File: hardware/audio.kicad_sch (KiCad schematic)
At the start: 5 parts, among them J10 AudioJack_PJ-342

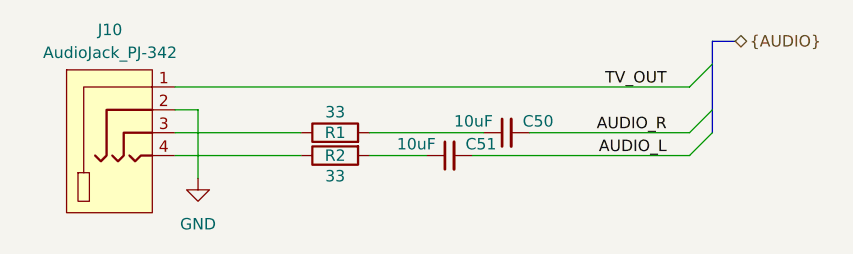
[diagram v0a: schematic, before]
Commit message: Finished DC DC converters and started decoupling the CPU
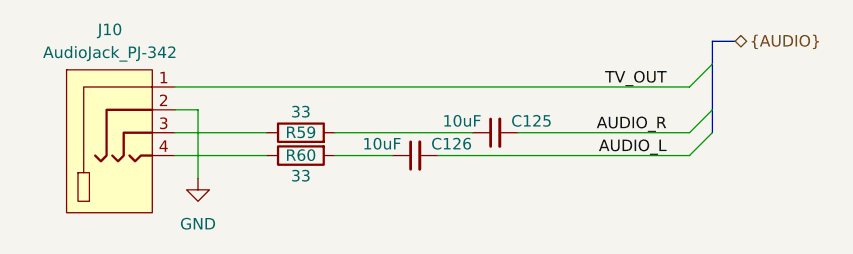
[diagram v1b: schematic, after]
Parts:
- renumbered C50 to C125, C51 to C126, R1 to R59, R2 to R60
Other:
- moved on the sheet: C125, C126, R59, R60
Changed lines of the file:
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@@
 	(wire
 		(pts
-			(xy 132.08 95.25) (xy 146.05 95.25)
-		)
-		(stroke
-			(width 0)
-			(type default)
-		)
-	)
-	(wire
-		(pts
-			(xy 165.1 95.25) (xy 189.23 95.25)
+			(xy 132.08 95.25) (xy 142.24 95.25)
+		)
+		(stroke
+			(width 0)
+			(type default)
+		)
+	)
+	(wire
+		(pts
+			(xy 161.29 95.25) (xy 189.23 95.25)
 		)
 		(stroke
@@
 	(wire
 		(pts
-			(xy 153.67 92.71) (xy 166.37 92.71)
+			(xy 149.86 92.71) (xy 165.1 92.71)
 		)
 		(stroke
@@
 	(wire
 		(pts
-			(xy 153.67 95.25) (xy 160.02 95.25)
+			(xy 149.86 95.25) (xy 156.21 95.25)
 		)
 		(stroke
@@
 	(wire
 		(pts
-			(xy 171.45 92.71) (xy 189.23 92.71)
+			(xy 170.18 92.71) (xy 189.23 92.71)
 		)
 		(stroke
@@
 	(wire
 		(pts
-			(xy 132.08 92.71) (xy 146.05 92.71)
+			(xy 132.08 92.71) (xy 142.24 92.71)
 		)
 		(stroke
@@
 	(symbol
 		(lib_id "Device:R")
-		(at 149.86 95.25 90)
+		(at 146.05 95.25 90)
 		(mirror x)
 		(unit 1)
@@
 		(on_board yes)
 		(dnp no)
-		(property "Reference" "R2"
-			(at 149.86 95.25 90)
+		(property "Reference" "R60"
+			(at 146.05 95.25 90)
 			(effects
 				(font
@@
 		)
 		(property "Value" "33"
-			(at 149.86 97.536 90)
+			(at 146.05 97.536 90)
 			(effects
 				(font
@@
 		)
 		(property "Footprint" "Resistor_SMD:R_0402_1005Metric"
-			(at 149.86 93.472 90)
+			(at 146.05 93.472 90)
 			(effects
 				(font
@@
 		)
 		(property "Datasheet" "~"
-			(at 149.86 95.25 0)
+			(at 146.05 95.25 0)
 			(effects
 				(font
@@
 		)
 		(property "Description" "Resistor"
-			(at 149.86 95.25 0)
+			(at 146.05 95.25 0)
 			(effects
 				(font
@@
 		)
 		(property "LCSC Part #" ""
-			(at 149.86 95.25 90)
+			(at 146.05 95.25 90)
 			(effects
 				(font
@@
 			(project "cm0"
 				(path "/b53f5dbb-8078-4818-9e8f-fdf90ba6d854/5ae223d4-d68f-4671-997c-b9179dc72885"
-					(reference "R2")
+					(reference "R60")
 					(unit 1)
 				)
@@
 	(symbol
 		(lib_id "Device:C_Small")
-		(at 168.91 92.71 90)
+		(at 167.64 92.71 90)
 		(unit 1)
 		(exclude_from_sim no)
@@
 		(on_board yes)
 		(dnp no)
-		(property "Reference" "C50"
-			(at 170.688 91.44 90)
+		(property "Reference" "C125"
+			(at 169.418 91.44 90)
 			(effects
 				(font
@@
 		)
 		(property "Value" "10uF"
-			(at 167.386 91.44 90)
+			(at 166.116 91.44 90)
 			(effects
 				(font
@@
 		)
 		(property "Footprint" "Capacitor_SMD:C_0603_1608Metric"
-			(at 168.91 92.71 0)
+			(at 167.64 92.71 0)
 			(effects
 				(font
@@
 		)
 		(property "Datasheet" "~"
-			(at 168.91 92.71 0)
+			(at 167.64 92.71 0)
 			(effects
 				(font
@@
 		)
 		(property "Description" "Unpolarized capacitor, small symbol"
-			(at 168.91 92.71 0)
+			(at 167.64 92.71 0)
 			(effects
 				(font
@@
 		)
 		(property "LCSC Part #" "C19702"
-			(at 168.91 92.71 0)
+			(at 167.64 92.71 0)
 			(effects
 				(font
@@
 			(project "cm0"
 				(path "/b53f5dbb-8078-4818-9e8f-fdf90ba6d854/5ae223d4-d68f-4671-997c-b9179dc72885"
-					(reference "C50")
+					(reference "C125")
 					(unit 1)
 				)
@@
 	(symbol
 		(lib_id "Device:R")
-		(at 149.86 92.71 90)
+		(at 146.05 92.71 90)
 		(unit 1)
 		(exclude_from_sim no)
@@
 		(on_board yes)
 		(dnp no)
-		(property "Reference" "R1"
-			(at 149.86 92.71 90)
+		(property "Reference" "R59"
+			(at 146.05 92.71 90)
 			(effects
 				(font
@@
 		)
 		(property "Value" "33"
-			(at 149.86 90.424 90)
+			(at 146.05 90.424 90)
 			(effects
 				(font
@@
 		)
 		(property "Footprint" "Resistor_SMD:R_0402_1005Metric"
-			(at 149.86 94.488 90)
+			(at 146.05 94.488 90)
 			(effects
 				(font
@@
 		)
 		(property "Datasheet" "~"
-			(at 149.86 92.71 0)
+			(at 146.05 92.71 0)
 			(effects
 				(font
@@
 		)
 		(property "Description" "Resistor"
-			(at 149.86 92.71 0)
+			(at 146.05 92.71 0)
 			(effects
 				(font
@@
 		)
 		(property "LCSC Part #" ""
-			(at 149.86 92.71 90)
+			(at 146.05 92.71 90)
 			(effects
 				(font
@@
 			(project "cm0"
 				(path "/b53f5dbb-8078-4818-9e8f-fdf90ba6d854/5ae223d4-d68f-4671-997c-b9179dc72885"
-					(reference "R1")
+					(reference "R59")
 					(unit 1)
 				)
@@
 	(symbol
 		(lib_id "Device:C_Small")
-		(at 162.56 95.25 90)
+		(at 158.75 95.25 90)
 		(unit 1)
 		(exclude_from_sim no)
@@
 		(on_board yes)
 		(dnp no)
-		(property "Reference" "C51"
-			(at 164.338 93.98 90)
+		(property "Reference" "C126"
+			(at 160.528 93.98 90)
 			(effects
 				(font
@@
 		)
 		(property "Value" "10uF"
-			(at 161.036 93.98 90)
+			(at 157.226 93.98 90)
 			(effects
 				(font
@@
 		)
 		(property "Footprint" "Capacitor_SMD:C_0603_1608Metric"
-			(at 162.56 95.25 0)
+			(at 158.75 95.25 0)
 			(effects
 				(font
@@
 		)
 		(property "Datasheet" "~"
-			(at 162.56 95.25 0)
+			(at 158.75 95.25 0)
 			(effects
 				(font
@@
 		)
 		(property "Description" "Unpolarized capacitor, small symbol"
-			(at 162.56 95.25 0)
+			(at 158.75 95.25 0)
 			(effects
 				(font
@@
 		)
 		(property "LCSC Part #" "C19702"
-			(at 162.56 95.25 0)
+			(at 158.75 95.25 0)
 			(effects
 				(font
@@
 			(project "cm0"
 				(path "/b53f5dbb-8078-4818-9e8f-fdf90ba6d854/5ae223d4-d68f-4671-997c-b9179dc72885"
-					(reference "C51")
+					(reference "C126")
 					(unit 1)
 				)
@@
 		(dnp no)
 		(fields_autoplaced yes)
-		(property "Reference" "#PWR078"
+		(property "Reference" "#PWR0156"
 			(at 134.62 104.14 0)
 			(effects
@@
 			(project ""
 				(path "/b53f5dbb-8078-4818-9e8f-fdf90ba6d854/5ae223d4-d68f-4671-997c-b9179dc72885"
-					(reference "#PWR078")
+					(reference "#PWR0156")
 					(unit 1)
 				)

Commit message: Decoupling on PCB side almost done
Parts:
- J10: FT Position Offset (none) -> -0.3175,0.4445
- R59, R60: LCSC Part # (none) -> C25105
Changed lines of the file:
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@@
 			)
 		)
-		(property "LCSC Part #" ""
+		(property "LCSC Part #" "C25105"
+			(at 146.05 95.25 90)
+			(effects
+				(font
+					(size 1.27 1.27)
+				)
+				(hide yes)
+			)
+		)
+		(property "FT Position Offset" ""
+			(at 146.05 95.25 90)
+			(effects
+				(font
+					(size 1.27 1.27)
+				)
+				(hide yes)
+			)
+		)
+		(property "FT Rotation Offset" ""
 			(at 146.05 95.25 90)
 			(effects
@@
 			)
 		)
+		(property "FT Position Offset" "-0.3175,0.4445"
+			(at 125.73 93.98 0)
+			(effects
+				(font
+					(size 1.27 1.27)
+				)
+				(hide yes)
+			)
+		)
+		(property "FT Rotation Offset" ""
+			(at 125.73 93.98 0)
+			(effects
+				(font
+					(size 1.27 1.27)
+				)
+				(hide yes)
+			)
+		)
 		(pin "4"
 		)
@@
 			)
 		)
+		(property "FT Position Offset" ""
+			(at 167.64 92.71 90)
+			(effects
+				(font
+					(size 1.27 1.27)
+				)
+				(hide yes)
+			)
+		)
+		(property "FT Rotation Offset" ""
+			(at 167.64 92.71 90)
+			(effects
+				(font
+					(size 1.27 1.27)
+				)
+				(hide yes)
+			)
+		)
 		(pin "1"
 		)
@@
 			)
 		)
-		(property "LCSC Part #" ""
+		(property "LCSC Part #" "C25105"
+			(at 146.05 92.71 90)
+			(effects
+				(font
+					(size 1.27 1.27)
+				)
+				(hide yes)
+			)
+		)
+		(property "FT Position Offset" ""
+			(at 146.05 92.71 90)
+			(effects
+				(font
+					(size 1.27 1.27)
+				)
+				(hide yes)
+			)
+		)
+		(property "FT Rotation Offset" ""
 			(at 146.05 92.71 90)
 			(effects
@@
 			(effects
 				(font
+					(size 1.27 1.27)
+				)
+				(hide yes)
+			)
+		)
+		(property "FT Position Offset" ""
+			(at 158.75 95.25 90)
+			(effects
+				(font
+					(size 1.27 1.27)
+				)
+				(hide yes)
+			)
+		)
+		(property "FT Rotation Offset" ""
+			(at 158.75 95.25 90)
+			(effects
+				(font

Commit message: 99%
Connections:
- net TV_OUT: no longer names the net of J10.1
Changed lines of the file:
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@@
-	)
-	(bus_entry
-		(at 189.23 87.63)
-		(size 2.54 -2.54)
-		(stroke
-			(width 0)
-			(type default)
-		)
 	)
 	(bus_entry
@@
 		)
 	)
-	(bus
-		(pts
-			(xy 191.77 90.17) (xy 191.77 85.09)
-		)
-		(stroke
-			(width 0)
-			(type default)
-		)
-	)
 	(wire
 		(pts
@@
 	(wire
 		(pts
-			(xy 132.08 87.63) (xy 189.23 87.63)
-		)
-		(stroke
-			(width 0)
-			(type default)
-		)
-	)
-	(wire
-		(pts
 			(xy 134.62 97.79) (xy 134.62 90.17)
-		)
-		(stroke
-			(width 0)
-			(type default)
-		)
-	)
-	(bus
-		(pts
-			(xy 191.77 85.09) (xy 191.77 82.55)
 		)
 		(stroke
@@
 	(bus
 		(pts
-			(xy 191.77 82.55) (xy 194.31 82.55)
+			(xy 191.77 90.17) (xy 194.31 90.17)
 		)
 		(stroke
@@
 		)
 	)
-	(label "TV_OUT"
-		(at 186.69 87.63 180)
-		(effects
-			(font
-				(size 1.27 1.27)
-			)
-			(justify right bottom)
-		)
-	)
 	(label "AUDIO_L"
 		(at 186.69 95.25 180)
@@
 	(hierarchical_label "{AUDIO}"
 		(shape bidirectional)
-		(at 194.31 82.55 0)
+		(at 194.31 90.17 0)
 		(effects
 			(font
